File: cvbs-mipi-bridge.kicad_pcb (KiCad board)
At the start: 4 copper layers, 55 x 70 mm, 105 parts, among them IC1 ADV7280BCPZ-M, IC2 TLV70018, IC4 SN74AUP1G17DCKR, IC5 SN74AUP1G17DCKR, J1 WE_68715014522, J2 61300211121, J3 KLPX-0848A-2-Y, J4 KLPX-0848A-2-Y, J5 KLPX-0848A-2-Y, J6 KLPX-0848A-2-Y, J7 61300211121, Q1 BSS138APW, Q2 BSS138APW, Q3 BSS138APW, Q4 BSS138APW, Y1 ABM8G-28.63636MHZ-18-D2Y-T

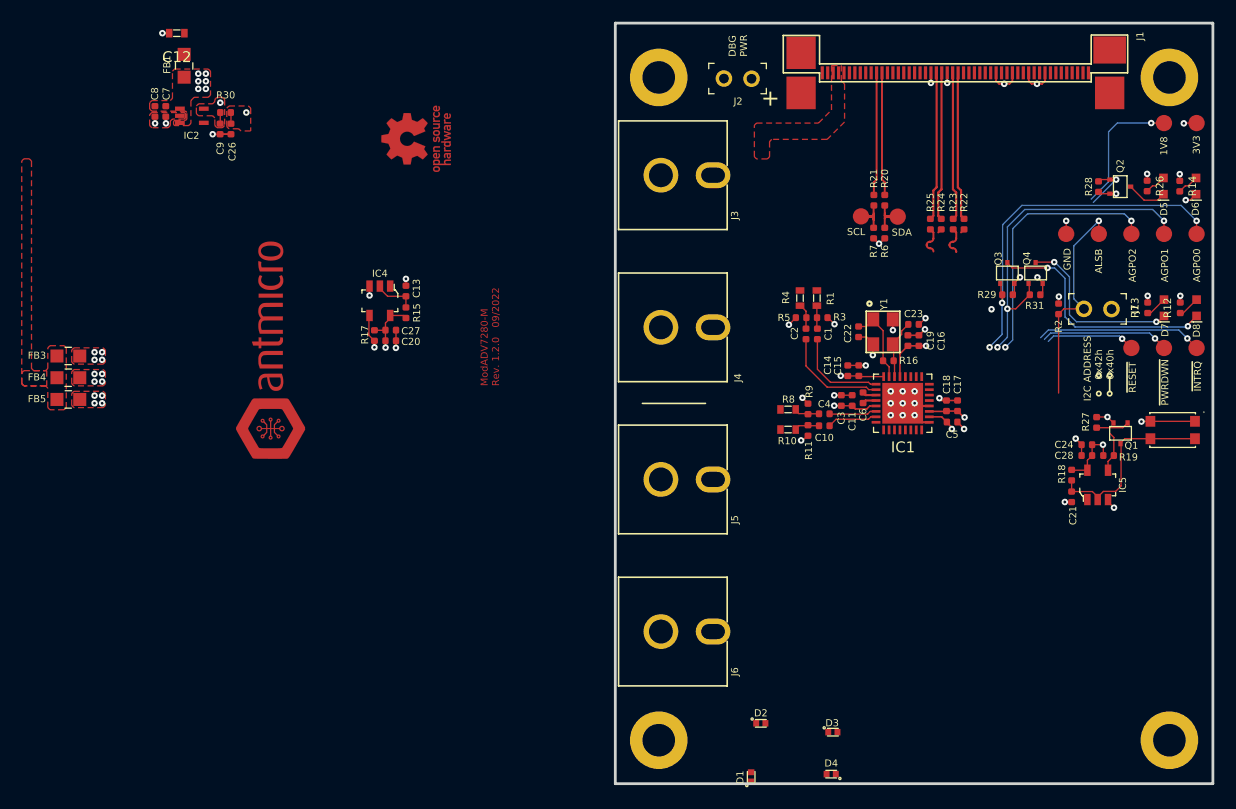
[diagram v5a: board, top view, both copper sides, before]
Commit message: Place components, route video signals
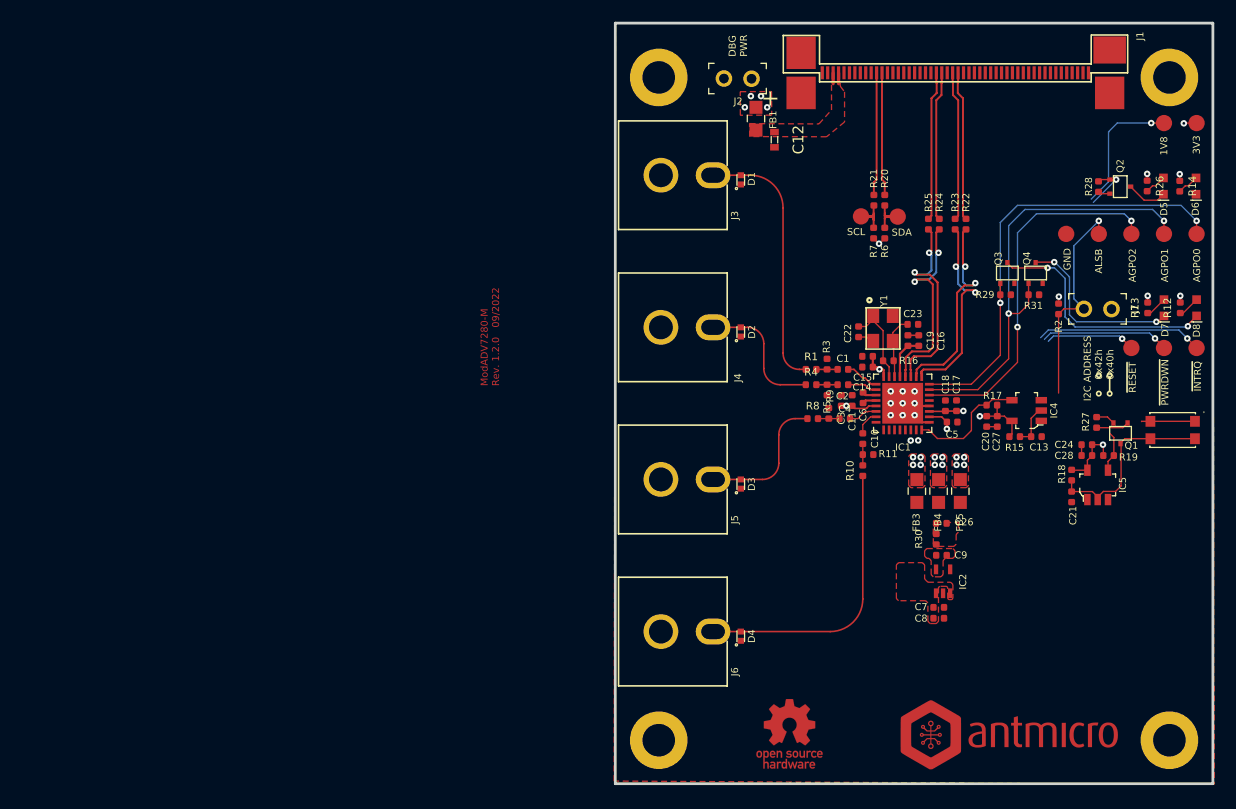
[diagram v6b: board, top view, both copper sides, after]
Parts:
- R1, R10, R4, R8: value R_24R_0603 -> R_24R_0402; footprint cvbs-mipi-bridge-footprints:0603-res -> antmicro-footprints:0402-res
- moved C8 85.9 mm to (141.5, 110.8), turned to 0 degrees
- moved C7 84.5 mm to (141.5, 109.8), turned to 180 degrees
- moved FB5 82.5 mm to (143.5, 99.1), turned to 90 degrees
- moved IC2 81.3 mm to (141.9, 107.4), turned to 0 degrees
- moved FB4 80.8 mm to (141.5, 99.1), turned to 90 degrees
- moved FB3 79.1 mm to (139.5, 99.1), turned to 90 degrees
- moved C9 77.1 mm to (141.7, 105.0), turned to 0 degrees
- moved N1 76.6 mm to (148.0, 121.7), turned to 0 degrees
- moved R30 76.3 mm to (141.2, 103.5), turned to 90 degrees
- moved C26 74.8 mm to (141.7, 102.0), turned to 180 degrees
- moved N2 64.7 mm to (127.7, 121.4), turned to 0 degrees
- moved IC4 60.4 mm to (149.6, 91.7), turned to 90 degrees
- moved C13 59.6 mm to (150.5, 94.1), turned to 0 degrees
- moved R17 57.2 mm to (146.4, 91.2), turned to 0 degrees
- moved R15 57.2 mm to (148.5, 94.1), turned to 180 degrees
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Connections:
- net Net-(C1-Pad1) renamed /AIN1_C
- net Net-(C10-Pad1) renamed /AIN4_C
- net Net-(C2-Pad1) renamed /AIN2_C
- net Net-(C4-Pad1) renamed /AIN3_C
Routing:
- net GND: track 50.3 -> 15.0 mm, vias 43 -> 9
- net /AIN4_ESD: track 0.00 -> 26.7 mm
- net /AIN1_ESD: track 0.00 -> 24.3 mm
- net /CSI_A_D0_N: track 0.39 -> 19.0 mm, vias 0 -> 2
- net /CSI_A_CLK_N: track 0.39 -> 19.0 mm, vias 0 -> 2
- net /CSI_A_CLK_P: track 2.84 -> 19.0 mm, vias 0 -> 2
- net /CSI_A_D0_P: track 2.89 -> 19.0 mm, vias 0 -> 2
- net /AIN3_ESD: track 0.00 -> 12.9 mm
- net /AIN2_ESD: track 0.00 -> 12.4 mm
- net Net-(IC1-Pad6): track 24.5 -> 34.3 mm
- net /AGPO1: track 31.9 -> 41.4 mm, vias 3 -> 2
- net /AGPO0: track 33.7 -> 42.2 mm, vias 3 -> 2
- net /PWRDWN: track 14.9 -> 22.8 mm, vias 2 -> 1
- net /AIN2: track 9.81 -> 2.58 mm
- net /AIN1: track 8.68 -> 3.13 mm
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- removed copper zone on In2.Cu, net GND

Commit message: Loclib
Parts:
- R1, R10, R4, R8: footprint antmicro-footprints:0402-res -> cvbs-mipi-bridge-footprints:0402-res
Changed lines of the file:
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@@
     )
   )
-  (footprint "antmicro-footprints:0402-res" (layer "F.Cu")
+  (footprint "cvbs-mipi-bridge-footprints:0402-res" (layer "F.Cu")
     (at 134.48 97.19 90)
     (descr "Resistor SMD 0402 (1005 Metric), square (rectangular) end terminal, IPC_7351 nominal, (Body size source: http://www.tortai-tech.com/upload/download/2011102023233369053.pdf), generated with kicad-footprint-generator")
@@
     (pad "2" smd roundrect locked (at 0.485 0 90) (size 0.59 0.64) (layers "F.Cu" "F.Paste" "F.Mask") (roundrect_rratio 0.25)
       (net 99 "/AIN4_C") (pintype "passive"))
-    (model "${ANT3DMDL}/0402-res.step"
+    (model "${KIPRJMOD}/lib/3d-models/0402-res.step"
       (offset (xyz 0 0 -0.01))
       (scale (xyz 1 1 1))
@@
     )
   )
-  (footprint "antmicro-footprints:0402-res" (layer "F.Cu")
+  (footprint "cvbs-mipi-bridge-footprints:0402-res" (layer "F.Cu")
     (at 129.72 87.87)
     (descr "Resistor SMD 0402 (1005 Metric), square (rectangular) end terminal, IPC_7351 nominal, (Body size source: http://www.tortai-tech.com/upload/download/2011102023233369053.pdf), generated with kicad-footprint-generator")
@@
     (pad "2" smd roundrect locked (at 0.485 0) (size 0.59 0.64) (layers "F.Cu" "F.Paste" "F.Mask") (roundrect_rratio 0.25)
       (net 96 "/AIN1_C") (pintype "passive"))
-    (model "${ANT3DMDL}/0402-res.step"
+    (model "${KIPRJMOD}/lib/3d-models/0402-res.step"
       (offset (xyz 0 0 -0.01))
       (scale (xyz 1 1 1))
@@
       (net 26 "/AGPO1") (pintype "passive"))
   )
-  (footprint "antmicro-footprints:0402-res" (layer "F.Cu")
+  (footprint "cvbs-mipi-bridge-footprints:0402-res" (layer "F.Cu")
     (at 129.72 89.28)
     (descr "Resistor SMD 0402 (1005 Metric), square (rectangular) end terminal, IPC_7351 nominal, (Body size source: http://www.tortai-tech.com/upload/download/2011102023233369053.pdf), generated with kicad-footprint-generator")
@@
     (pad "2" smd roundrect locked (at 0.485 0) (size 0.59 0.64) (layers "F.Cu" "F.Paste" "F.Mask") (roundrect_rratio 0.25)
       (net 97 "/AIN2_C") (pintype "passive"))
-    (model "${ANT3DMDL}/0402-res.step"
+    (model "${KIPRJMOD}/lib/3d-models/0402-res.step"
       (offset (xyz 0 0 -0.01))
       (scale (xyz 1 1 1))
@@
     )
   )
-  (footprint "antmicro-footprints:0402-res" (layer "F.Cu")
+  (footprint "cvbs-mipi-bridge-footprints:0402-res" (layer "F.Cu")
     (at 129.87 92.4)
     (descr "Resistor SMD 0402 (1005 Metric), square (rectangular) end terminal, IPC_7351 nominal, (Body size source: http://www.tortai-tech.com/upload/download/2011102023233369053.pdf), generated with kicad-footprint-generator")
@@
     (pad "2" smd roundrect locked (at 0.485 0) (size 0.59 0.64) (layers "F.Cu" "F.Paste" "F.Mask") (roundrect_rratio 0.25)
       (net 98 "/AIN3_C") (pintype "passive"))
-    (model "${ANT3DMDL}/0402-res.step"
+    (model "${KIPRJMOD}/lib/3d-models/0402-res.step"
       (offset (xyz 0 0 -0.01))
       (scale (xyz 1 1 1))

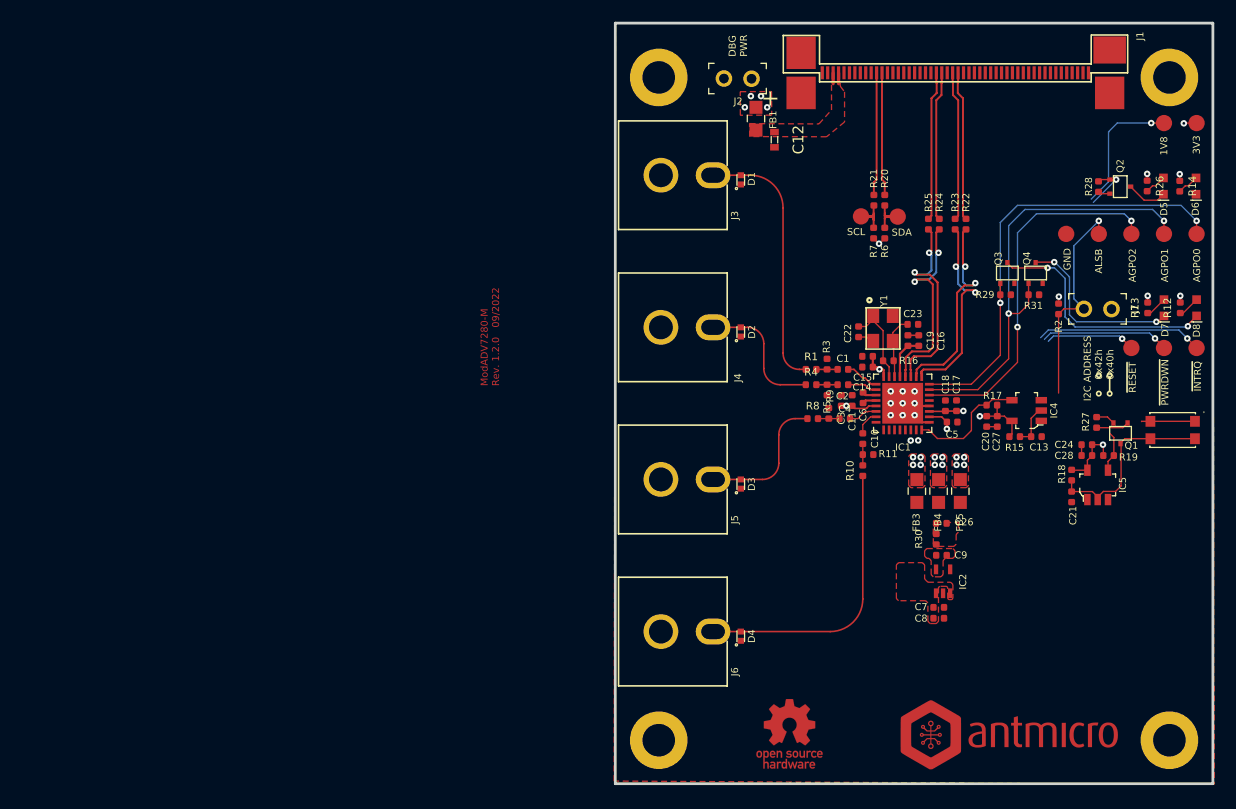
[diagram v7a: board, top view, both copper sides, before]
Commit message: Replace DC power connector
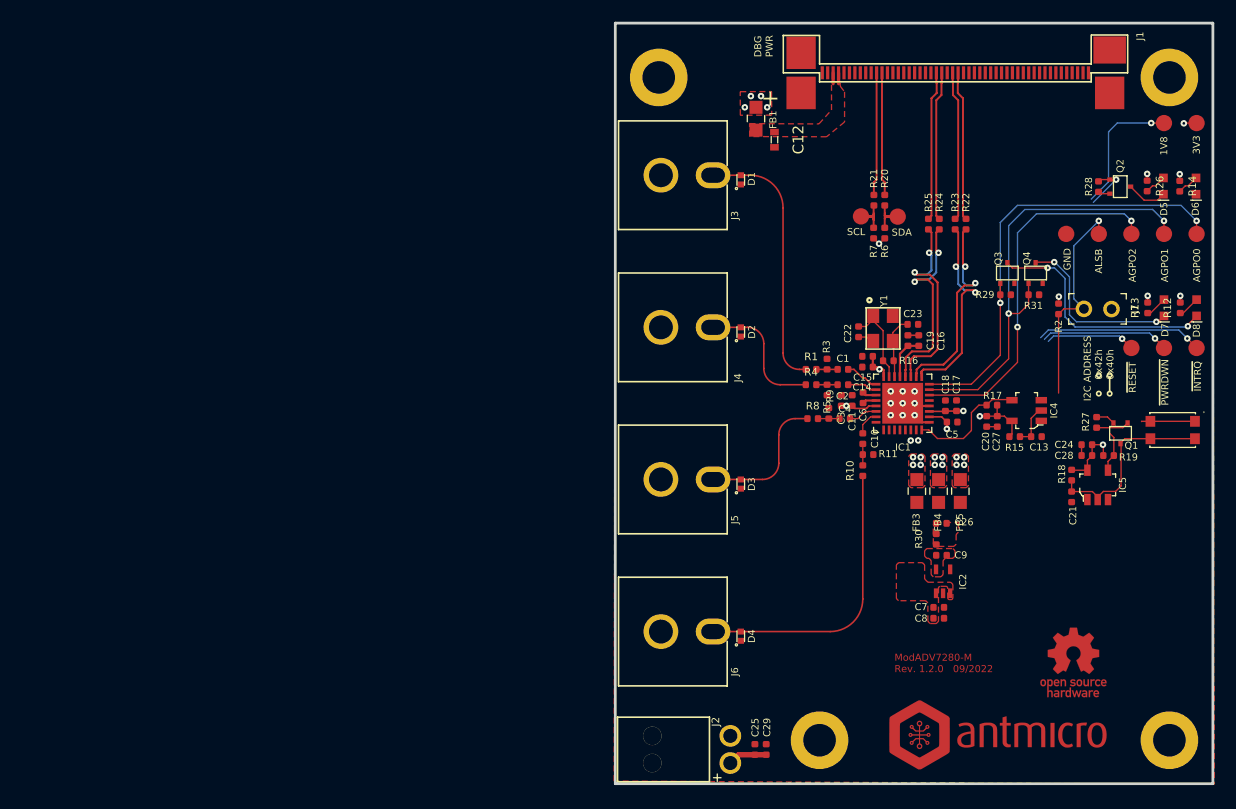
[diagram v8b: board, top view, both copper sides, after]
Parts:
- added C25: C_1u_0402, cvbs-mipi-bridge-footprints:0402-cap, F.Cu at (124.5, 122.8)
- added C29: C_100n_0402, cvbs-mipi-bridge-footprints:0402-cap, F.Cu at (125.6, 122.8)
- J2: value 61300211121 -> 1053131102; footprint cvbs-mipi-bridge-footprints:PinHeader_1x2_P2.54_Drill0.9mm -> cvbs-mipi-bridge-footprints:1053131102
- moved J2 61.8 mm to (122.3, 122.8), turned to -90 degrees
- moved N2 26.9 mm to (153.9, 114.8)
- moved MP2 14.9 mm to (130.6, 122.2)
- moved N1 1.04 mm to (146.9, 121.7)
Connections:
- J2 pad 1: GND -> 3V3_SYS
- J2 pad 2: 3V3_SYS -> GND
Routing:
- net 3V3_SYS: track 19.6 -> 23.2 mm
